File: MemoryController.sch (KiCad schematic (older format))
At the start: 10 parts, among them U10 74LVC1G74, U12 74AHC244, U15 74AHC1G04, U21 74AHC244, U22 74CBTLV16212

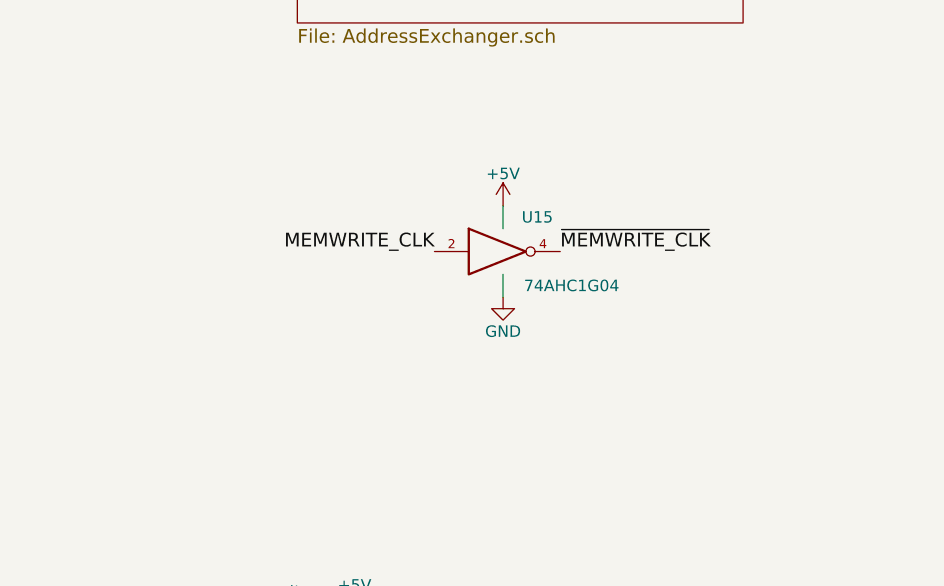
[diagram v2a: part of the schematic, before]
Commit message: Multiple change : Replacing old custom "LTC6994-1" symbol with the Kicad symbol "LTC6994xS6-1" Replacing old custom "LM810" symbol with the Kicad symbol "LM810" Replacing all hidden power pins symbols (hidden pins bug) Renaming "Main connector" to "SPS1 Processor connector" Removing old symbols, cleaning Replacing symbol "CD74AC238" with a new one
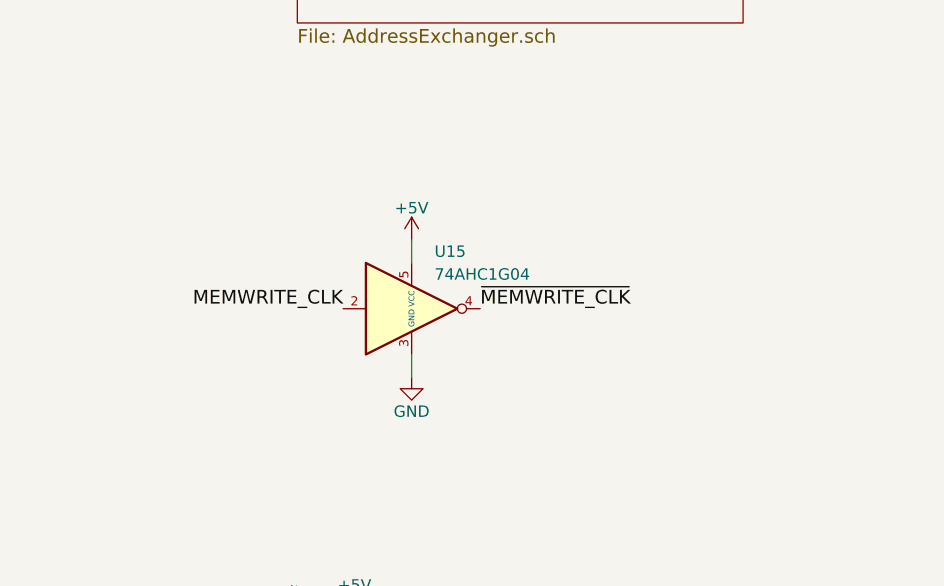
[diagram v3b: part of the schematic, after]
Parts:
- removed U15: 74AHC1G04, Package_TO_SOT_SMD:SOT-23-5, symbol 74xGxx:74AHC1G04
- added U15: 74AHC1G04, symbol Custom:74AHC1G04
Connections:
- net +5V: now also U15.5 (VCC)
- net GND: now also U15.3 (GND)
- net MEMWRITE_CLK: now also U15.2
- net ~MEMWRITE_CLK: now also U15.4
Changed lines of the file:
@@
 L power:+5V #PWR?
 U 1 1 5D3758ED
-P 4450 2400
+P 4050 2550
 AR Path="/5D3758ED" Ref="#PWR?"  Part="1"
 AR Path="/5BF276EA/5C3C5768/5D3758ED" Ref="#PWR?"  Part="1"
 AR Path="/5B965978/5D3758ED" Ref="#PWR0121"  Part="1"
-F 0 "#PWR0121" H 4450 2250 50  0001 C CNN
-F 1 "+5V" H 4450 2540 50  0000 C CNN
-F 2 "" H 4450 2400 50  0001 C CNN
-F 3 "" H 4450 2400 50  0001 C CNN
-	1    4450 2400
+F 0 "#PWR0121" H 4050 2400 50  0001 C CNN
+F 1 "+5V" H 4050 2690 50  0000 C CNN
+F 2 "" H 4050 2550 50  0001 C CNN
+F 3 "" H 4050 2550 50  0001 C CNN
+	1    4050 2550
 	1    0    0    -1
 $EndComp
@@
 L power:GND #PWR?
 U 1 1 5D3758F3
-P 4450 2800
+P 4050 3150
 AR Path="/5D3758F3" Ref="#PWR?"  Part="1"
 AR Path="/5BF276EA/5C3C5768/5D3758F3" Ref="#PWR?"  Part="1"
 AR Path="/5B965978/5D3758F3" Ref="#PWR0122"  Part="1"
-F 0 "#PWR0122" H 4450 2550 50  0001 C CNN
-F 1 "GND" H 4450 2650 50  0000 C CNN
-F 2 "" H 4450 2800 50  0001 C CNN
-F 3 "" H 4450 2800 50  0001 C CNN
-	1    4450 2800
-	1    0    0    -1
-$EndComp
-Wire Wire Line
-	4450 2800 4450 2700
-Wire Wire Line
-	4450 2500 4450 2400
-$Comp
-L 74xGxx:74AHC1G04 U?
-U 1 1 5D3758FD
-P 4450 2600
-AR Path="/5BF276EA/5C3C5768/5D3758FD" Ref="U?"  Part="1"
-AR Path="/5B965978/5D3758FD" Ref="U15"  Part="1"
-F 0 "U15" H 4600 2750 50  0000 C CNN
-F 1 "74AHC1G04" H 4750 2450 50  0000 C CNN
-F 2 "Package_TO_SOT_SMD:SOT-23-5" H 4450 2600 50  0001 C CNN
-F 3 "http://www.ti.com/lit/sg/scyt129e/scyt129e.pdf" H 4450 2600 50  0001 C CNN
-	1    4450 2600
-	1    0    0    -1
-$EndComp
-Text Label 4150 2600 2    60   ~ 0
+F 0 "#PWR0122" H 4050 2900 50  0001 C CNN
+F 1 "GND" H 4050 3000 50  0000 C CNN
+F 2 "" H 4050 3150 50  0001 C CNN
+F 3 "" H 4050 3150 50  0001 C CNN
+	1    4050 3150
+	1    0    0    -1
+$EndComp
+Text Label 3750 2850 2    60   ~ 0
 MEMWRITE_CLK
-Text Label 4700 2600 0    60   ~ 0
+Text Label 4350 2850 0    60   ~ 0
 ~MEMWRITE_CLK
 Text Label 7950 3650 2    60   ~ 0
@@
 Text Label 10050 6350 2    60   ~ 0
 SRCSET_CLK
+$Comp
+L Custom:74AHC1G04 U?
+U 1 1 5F93C019
+P 4050 2850
+AR Path="/5F93C019" Ref="U?"  Part="1"
+AR Path="/5B965978/5F93C019" Ref="U15"  Part="1"
+F 0 "U15" H 4150 3100 50  0000 L CNN
+F 1 "74AHC1G04" H 4150 3000 50  0000 L CNN
+F 2 "" H 4050 2850 50  0001 C CNN
+F 3 "https://assets.nexperia.com/documents/data-sheet/74AHC_AHCT1G04.pdf" H 4050 2850 50  0001 C CNN
+	1    4050 2850
+	1    0    0    -1
+$EndComp
+Wire Wire Line
+	4050 3150 4050 3050
+Wire Wire Line
+	4050 2650 4050 2550
 Wire Bus Line
 	1500 4400 1500 5200

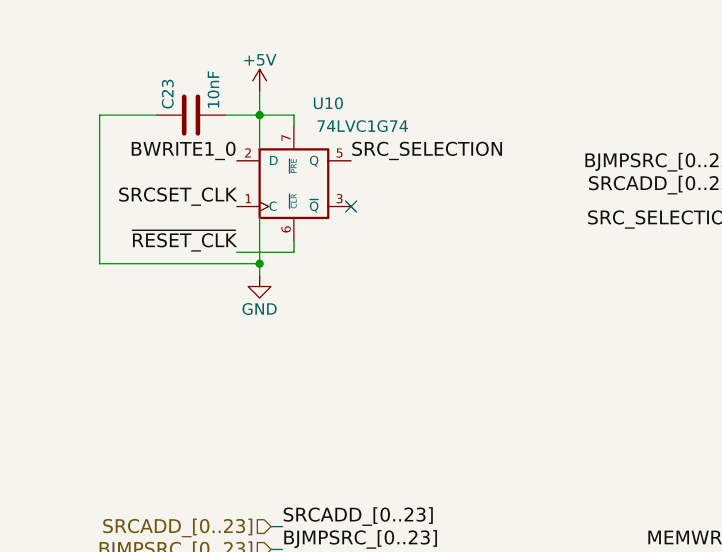
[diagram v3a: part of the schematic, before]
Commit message: replacing 74LVC1G74 symbol
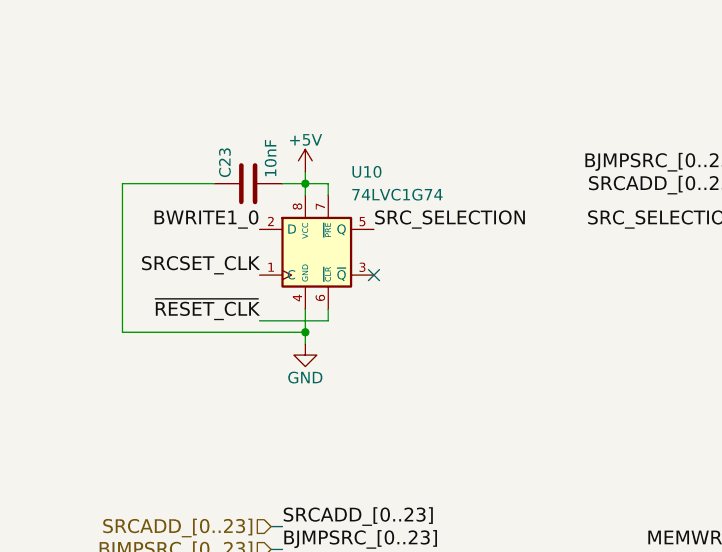
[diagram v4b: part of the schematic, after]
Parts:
- removed U10: 74LVC1G74, Package_SO:VSSOP-8_2.4x2.1mm_P0.5mm, symbol 74xGxx:74AUC1G74
- added U10: 74LVC1G74, symbol Custom:74LVC1G74
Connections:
- net +5V: now also U10.7 (~PRE), U10.8 (VCC)
- net BWRITE1_0: now also U10.2 (D)
- net GND: now also U10.4 (GND)
- net SRCSET_CLK: now also U10.1 (C)
- net SRC_SELECTION: now also U10.5 (Q)
- net ~RESET_CLK: now also U10.6 (~CLR)
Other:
- moved on the sheet: C23
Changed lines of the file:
@@
 Wire Wire Line
 	4500 5300 5850 5300
-$Comp
-L 74xGxx:74AUC1G74 U10
-U 1 1 5D5A688A
-P 1550 1250
-F 0 "U10" H 1700 1600 50  0000 C CNN
-F 1 "74LVC1G74" H 1850 1500 50  0000 C CNN
-F 2 "Package_SO:VSSOP-8_2.4x2.1mm_P0.5mm" H 1550 1250 50  0001 C CNN
-F 3 "http://www.ti.com/lit/sg/scyt129e/scyt129e.pdf" H 1550 1250 50  0001 C CNN
-	1    1550 1250
-	1    0    0    -1
-$EndComp
-Text Label 1800 1150 0    60   ~ 0
+Text Label 1900 1450 0    60   ~ 0
 SRC_SELECTION
 $Comp
 L power:+5V #PWR?
 U 1 1 5D5ACDBA
-P 1400 850
+P 1600 1200
 AR Path="/5A97A24B/5D5ACDBA" Ref="#PWR?"  Part="1"
 AR Path="/5B965978/5D5ACDBA" Ref="#PWR0124"  Part="1"
 AR Path="/5D5ACDBA" Ref="#PWR?"  Part="1"
-F 0 "#PWR0124" H 1400 700 50  0001 C CNN
-F 1 "+5V" H 1400 990 50  0000 C CNN
-F 2 "" H 1400 850 50  0001 C CNN
-F 3 "" H 1400 850 50  0001 C CNN
-	1    1400 850
-	1    0    0    -1
-$EndComp
-Wire Wire Line
-	1400 1100 1400 950
-Wire Wire Line
-	1550 1000 1550 950
-Wire Wire Line
-	1550 950  1400 950
-Connection ~ 1400 950
-Wire Wire Line
-	1400 950  1400 850
+F 0 "#PWR0124" H 1600 1050 50  0001 C CNN
+F 1 "+5V" H 1600 1340 50  0000 C CNN
+F 2 "" H 1600 1200 50  0001 C CNN
+F 3 "" H 1600 1200 50  0001 C CNN
+	1    1600 1200
+	1    0    0    -1
+$EndComp
+Wire Wire Line
+	1600 1300 1600 1250
 $Comp
 L power:GND #PWR?
 U 1 1 5D5C9F01
-P 1400 1650
+P 1600 1950
 AR Path="/5D5C9F01" Ref="#PWR?"  Part="1"
 AR Path="/5B965978/5D5C9F01" Ref="#PWR0125"  Part="1"
-F 0 "#PWR0125" H 1400 1400 50  0001 C CNN
-F 1 "GND" H 1400 1500 50  0000 C CNN
-F 2 "" H 1400 1650 50  0001 C CNN
-F 3 "" H 1400 1650 50  0001 C CNN
-	1    1400 1650
+F 0 "#PWR0125" H 1600 1700 50  0001 C CNN
+F 1 "GND" H 1600 1800 50  0000 C CNN
+F 2 "" H 1600 1950 50  0001 C CNN
+F 3 "" H 1600 1950 50  0001 C CNN
+	1    1600 1950
 	1    0    0    -1
 $EndComp
@@
 L Device:C C?
 U 1 1 5D5E7959
-P 1100 950
+P 1350 1250
 AR Path="/5A97A24B/5D5E7959" Ref="C?"  Part="1"
 AR Path="/5B965978/5D5E7959" Ref="C23"  Part="1"
 AR Path="/5D5E7959" Ref="C?"  Part="1"
-F 0 "C23" H 1125 1050 50  0000 L CNN
-F 1 "10nF" H 1125 850 50  0000 L CNN
-F 2 "Capacitor_SMD:C_0805_2012Metric" H 1138 800 50  0001 C CNN
-F 3 "" H 1100 950 50  0001 C CNN
-	1    1100 950
+F 0 "C23" H 1375 1350 50  0000 L CNN
+F 1 "10nF" H 1375 1150 50  0000 L CNN
+F 2 "Capacitor_SMD:C_0805_2012Metric" H 1388 1100 50  0001 C CNN
+F 3 "" H 1350 1250 50  0001 C CNN
+	1    1350 1250
 	0    -1   -1   0
 $EndComp
-Text Label 1300 1150 2    60   ~ 0
+Text Label 1400 1450 2    60   ~ 0
 BWRITE1_0
-Text Label 1300 1350 2    60   ~ 0
+Text Label 1400 1650 2    60   ~ 0
 SRCSET_CLK
-Wire Wire Line
-	1400 1400 1400 1600
-Text Label 1300 1550 2    60   ~ 0
+Text Label 1400 1850 2    60   ~ 0
 ~RESET_CLK
-Wire Wire Line
-	1300 1550 1550 1550
-Wire Wire Line
-	1550 1550 1550 1500
-NoConn ~ 1800 1350
-Wire Wire Line
-	1400 950  1250 950
-Wire Wire Line
-	950  950  700  950
-Wire Wire Line
-	700  950  700  1600
-Wire Wire Line
-	700  1600 1400 1600
-Connection ~ 1400 1600
-Wire Wire Line
-	1400 1600 1400 1650
 $Comp
 L Device:C C?
@@
 Wire Wire Line
 	4050 2650 4050 2550
+$Comp
+L Custom:74LVC1G74 U10
+U 1 1 5F7589E8
+P 1650 1550
+F 0 "U10" H 1800 1900 50  0000 L CNN
+F 1 "74LVC1G74" H 1800 1800 50  0000 L CNN
+F 2 "" H 1650 1550 50  0001 C CNN
+F 3 "http://www.ti.com/lit/sg/scyt129e/scyt129e.pdf" H 1650 1550 50  0001 C CNN
+	1    1650 1550
+	1    0    0    -1
+$EndComp
+Wire Wire Line
+	1600 1250 1700 1250
+Wire Wire Line
+	1700 1250 1700 1300
+Connection ~ 1600 1250
+Wire Wire Line
+	1600 1250 1600 1200
+Wire Wire Line
+	1700 1800 1700 1850
+Wire Wire Line
+	1700 1850 1400 1850
+NoConn ~ 1900 1650
+Wire Wire Line
+	1600 1800 1600 1900
+Wire Wire Line
+	1600 1900 800  1900
+Wire Wire Line
+	800  1900 800  1250
+Wire Wire Line
+	800  1250 1200 1250
+Connection ~ 1600 1900
+Wire Wire Line
+	1600 1900 1600 1950
+Wire Wire Line
+	1500 1250 1600 1250
 Wire Bus Line
 	1500 4400 1500 5200
